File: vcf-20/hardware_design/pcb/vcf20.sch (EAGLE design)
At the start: 59 parts, among them IC1 LM13700M, J1 WQP-PJ301M-12_JACK, J2 WQP-PJ301M-12_JACK, J3 WQP-PJ301M-12_JACK, J4 WQP-PJ301M-12_JACK, T1 3904, T2 3904, U1 TL072AD, U2 TL072AD, U3 NE5532D

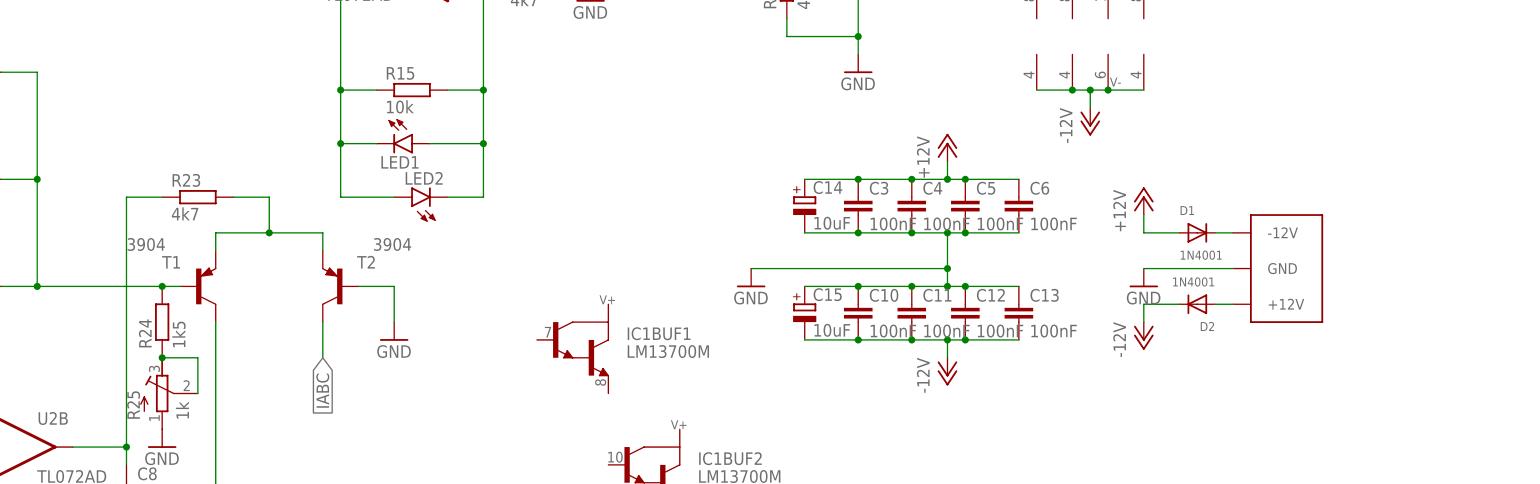
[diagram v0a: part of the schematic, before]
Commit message: Fix reversed power connector for vcf-20
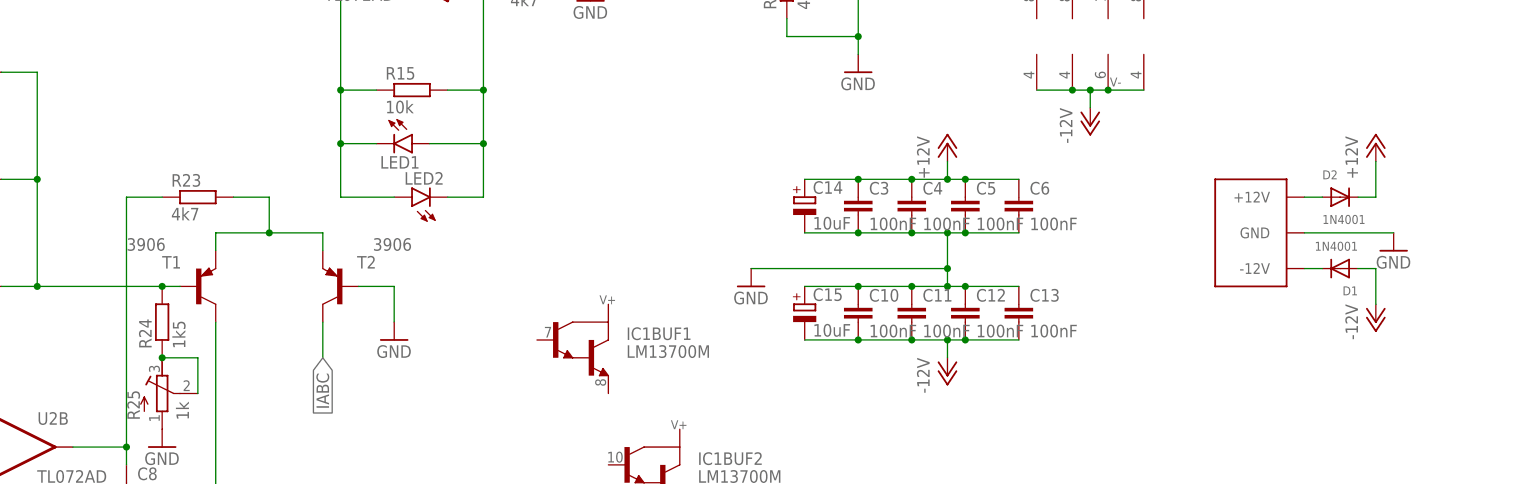
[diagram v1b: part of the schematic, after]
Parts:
- T1, T2: value 3904 -> 3906
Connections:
- net +12V: now also D2.C; no longer D1.A
- net -12V: now also D1.A; no longer D2.C
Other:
- moved on the sheet: D1, D2
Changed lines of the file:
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@@
 <part name="R20" library="jhbruhn-cr" deviceset="R-EU_" device="R0402" package3d_urn="urn:adsk.eagle:package:23547/3" value="100k"/>
 <part name="R21" library="jhbruhn-cr" deviceset="R-EU_" device="R0402" package3d_urn="urn:adsk.eagle:package:23547/3" value="220k"/>
-<part name="T1" library="transistor" library_urn="urn:adsk.eagle:library:402" deviceset="*-PNP-" device="SOT23-BEC" package3d_urn="urn:adsk.eagle:package:28748/2" technology="MMBT3906LT1" value="3904"/>
-<part name="T2" library="transistor" library_urn="urn:adsk.eagle:library:402" deviceset="*-PNP-" device="SOT23-BEC" package3d_urn="urn:adsk.eagle:package:28748/2" technology="MMBT3906LT1" value="3904"/>
+<part name="T1" library="transistor" library_urn="urn:adsk.eagle:library:402" deviceset="*-PNP-" device="SOT23-BEC" package3d_urn="urn:adsk.eagle:package:28748/2" technology="MMBT3906LT1" value="3906"/>
+<part name="T2" library="transistor" library_urn="urn:adsk.eagle:library:402" deviceset="*-PNP-" device="SOT23-BEC" package3d_urn="urn:adsk.eagle:package:28748/2" technology="MMBT3906LT1" value="3906"/>
 <part name="P-2" library="supply1" library_urn="urn:adsk.eagle:library:371" deviceset="-12V" device=""/>
 <part name="R22" library="jhbruhn-cr" deviceset="R-EU_" device="R0402" package3d_urn="urn:adsk.eagle:package:23547/3" value="470k"/>
@@
 <attribute name="VALUE" x="114.3" y="-50.8" size="1.778" layer="96"/>
 </instance>
-<instance part="C9" gate="G$1" x="274.32" y="-22.86" smashed="yes" rot="R180"/>
+<instance part="C9" gate="G$1" x="274.32" y="-17.78" smashed="yes"/>
 <instance part="C10" gate="G$1" x="215.9" y="-27.94" smashed="yes">
 <attribute name="NAME" x="217.424" y="-27.559" size="1.778" layer="95"/>
@@
 <attribute name="VALUE" x="198.12" y="-27.94" size="1.778" layer="96"/>
 </instance>
-<instance part="D1" gate="G$1" x="264.16" y="-17.78" smashed="yes">
-<attribute name="NAME" x="261.62" y="-15.24" size="1.27" layer="95"/>
-<attribute name="VALUE" x="261.62" y="-21.59" size="1.27" layer="96"/>
-</instance>
-<instance part="D2" gate="G$1" x="264.16" y="-27.94" smashed="yes" rot="R180">
-<attribute name="NAME" x="266.7" y="-30.48" size="1.27" layer="95" rot="R180"/>
-<attribute name="VALUE" x="266.7" y="-24.13" size="1.27" layer="96" rot="R180"/>
-</instance>
-<instance part="P+3" gate="1" x="256.54" y="-12.7" smashed="yes">
-<attribute name="VALUE" x="254" y="-17.78" size="1.778" layer="96" rot="R90"/>
-</instance>
-<instance part="P-4" gate="1" x="256.54" y="-33.02" smashed="yes">
-<attribute name="VALUE" x="254" y="-35.56" size="1.778" layer="96" rot="R90"/>
-</instance>
-<instance part="GND18" gate="1" x="256.54" y="-25.4" smashed="yes">
-<attribute name="VALUE" x="254" y="-27.94" size="1.778" layer="96"/>
+<instance part="D1" gate="G$1" x="284.48" y="-22.86" smashed="yes" rot="R180">
+<attribute name="NAME" x="287.02" y="-25.4" size="1.27" layer="95" rot="R180"/>
+<attribute name="VALUE" x="287.02" y="-19.05" size="1.27" layer="96" rot="R180"/>
+</instance>
+<instance part="D2" gate="G$1" x="284.48" y="-12.7" smashed="yes">
+<attribute name="NAME" x="281.94" y="-10.16" size="1.27" layer="95"/>
+<attribute name="VALUE" x="281.94" y="-16.51" size="1.27" layer="96"/>
+</instance>
+<instance part="P+3" gate="1" x="289.56" y="-5.08" smashed="yes">
+<attribute name="VALUE" x="287.02" y="-10.16" size="1.778" layer="96" rot="R90"/>
+</instance>
+<instance part="P-4" gate="1" x="289.56" y="-30.48" smashed="yes">
+<attribute name="VALUE" x="287.02" y="-33.02" size="1.778" layer="96" rot="R90"/>
+</instance>
+<instance part="GND18" gate="1" x="292.1" y="-20.32" smashed="yes">
+<attribute name="VALUE" x="289.56" y="-22.86" size="1.778" layer="96"/>
 </instance>
 <instance part="C14" gate="G$1" x="208.28" y="-12.7" smashed="yes">
@@
 <pinref part="C9" gate="G$1" pin="GND"/>
 <pinref part="GND18" gate="1" pin="GND"/>
-<wire x1="269.24" y1="-22.86" x2="256.54" y2="-22.86" width="0.1524" layer="91"/>
+<wire x1="279.4" y1="-17.78" x2="292.1" y2="-17.78" width="0.1524" layer="91"/>
 </segment>
 </net>
@@
 </segment>
 <segment>
-<pinref part="D1" gate="G$1" pin="A"/>
-<wire x1="261.62" y1="-17.78" x2="256.54" y2="-17.78" width="0.1524" layer="91"/>
-<pinref part="P+3" gate="1" pin="+12V"/>
-<wire x1="256.54" y1="-17.78" x2="256.54" y2="-15.24" width="0.1524" layer="91"/>
-</segment>
-<segment>
 <pinref part="U1" gate="P" pin="V+"/>
 <pinref part="U2" gate="P" pin="V+"/>
@@
 <wire x1="248.92" y1="20.32" x2="248.92" y2="17.78" width="0.1524" layer="91"/>
 <junction x="248.92" y="17.78"/>
+</segment>
+<segment>
+<pinref part="D2" gate="G$1" pin="C"/>
+<pinref part="P+3" gate="1" pin="+12V"/>
+<wire x1="287.02" y1="-12.7" x2="289.56" y2="-12.7" width="0.1524" layer="91"/>
+<wire x1="289.56" y1="-12.7" x2="289.56" y2="-7.62" width="0.1524" layer="91"/>
 </segment>
 </net>
@@
 </segment>
 <segment>
-<pinref part="D2" gate="G$1" pin="C"/>
-<wire x1="261.62" y1="-27.94" x2="256.54" y2="-27.94" width="0.1524" layer="91"/>
-<pinref part="P-4" gate="1" pin="-12V"/>
-<wire x1="256.54" y1="-27.94" x2="256.54" y2="-30.48" width="0.1524" layer="91"/>
-</segment>
-<segment>
 <pinref part="U1" gate="P" pin="V-"/>
 <pinref part="U2" gate="P" pin="V-"/>
@@
 <wire x1="248.92" y1="0" x2="248.92" y2="2.54" width="0.1524" layer="91"/>
 <junction x="248.92" y="2.54"/>
+</segment>
+<segment>
+<pinref part="D1" gate="G$1" pin="A"/>
+<wire x1="287.02" y1="-22.86" x2="289.56" y2="-22.86" width="0.1524" layer="91"/>
+<pinref part="P-4" gate="1" pin="-12V"/>
+<wire x1="289.56" y1="-22.86" x2="289.56" y2="-27.94" width="0.1524" layer="91"/>
 </segment>
 </net>
@@
 <pinref part="C9" gate="G$1" pin="+12V"/>
 <pinref part="D2" gate="G$1" pin="A"/>
-<wire x1="269.24" y1="-27.94" x2="266.7" y2="-27.94" width="0.1524" layer="91"/>
+<wire x1="279.4" y1="-12.7" x2="281.94" y2="-12.7" width="0.1524" layer="91"/>
 </segment>
 </net>
@@
 <pinref part="C9" gate="G$1" pin="-12V"/>
 <pinref part="D1" gate="G$1" pin="C"/>
-<wire x1="269.24" y1="-17.78" x2="266.7" y2="-17.78" width="0.1524" layer="91"/>
-</segment>
-</net>
+<wire x1="279.4" y1="-22.86" x2="281.94" y2="-22.86" width="0.1524" layer="91"/>
+</segment>
+</net>
